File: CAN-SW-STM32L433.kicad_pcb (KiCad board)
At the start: 2 copper layers, 70 x 53 mm, 37 parts, among them J1 H GND L, J2 TERM, J3 UART1, J4 SWLINK, J5 CENTER +12V, U1 STM32L433RCT3, U2 MCP2562-E-SN

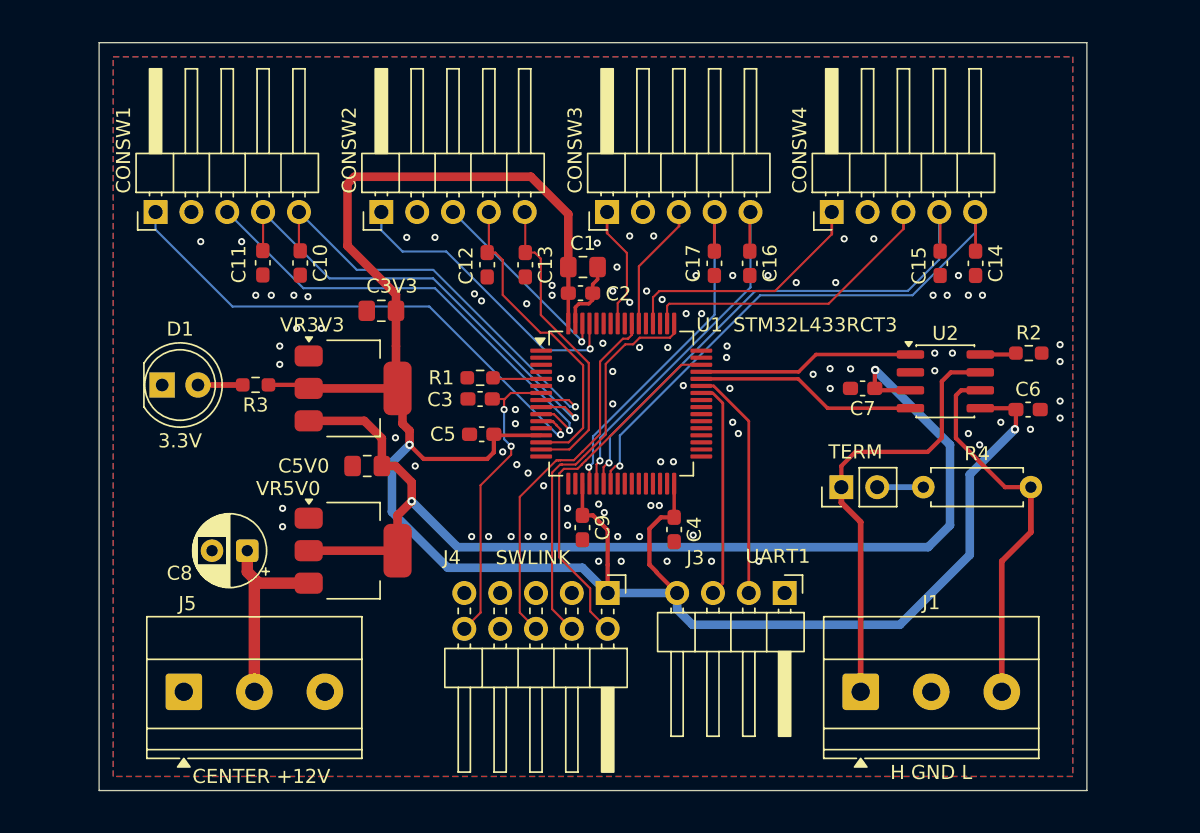
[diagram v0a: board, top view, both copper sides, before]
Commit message: added status led and tvs diode
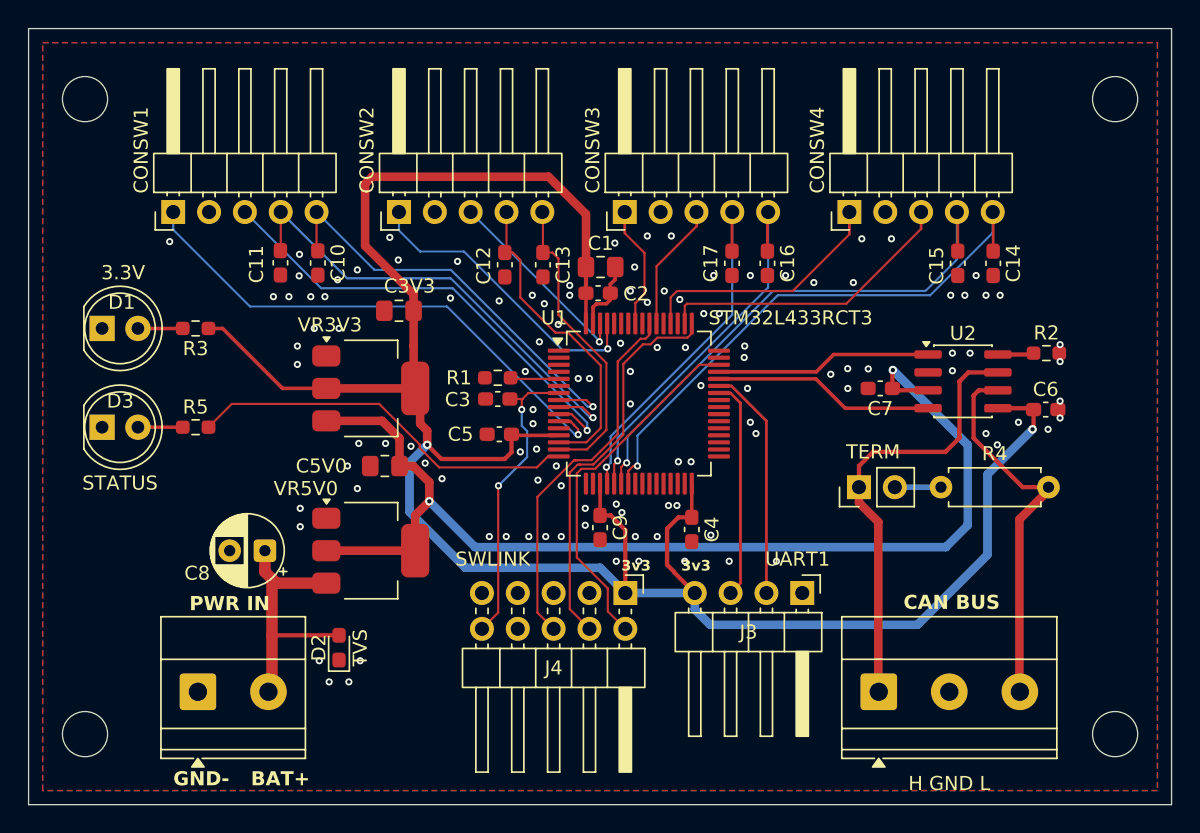
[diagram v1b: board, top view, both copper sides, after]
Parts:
- added D2: TVS, Diode_SMD:D_0603_1608Metric_Pad1.05x0.95mm_HandSolder, F.Cu at (119.0, 118.9)
- added D3: STATUS, LED_THT:LED_D5.0mm_Clear, F.Cu at (102.2, 103.2)
- added H1: MountingHole, MountingHole:MountingHole_3.2mm_M3_DIN965, F.Cu at (101.0, 80.0)
- added H2: MountingHole, MountingHole:MountingHole_3.2mm_M3_DIN965, F.Cu at (174.0, 80.0)
- added H3: MountingHole, MountingHole:MountingHole_3.2mm_M3_DIN965, F.Cu at (101.0, 125.0)
- added H4: MountingHole, MountingHole:MountingHole_3.2mm_M3_DIN965, F.Cu at (174.0, 125.0)
- added R5: 1K, Resistor_SMD:R_0603_1608Metric_Pad0.98x0.95mm_HandSolder, F.Cu at (108.8, 103.2)
- J5: value CENTER +12V -> PWR IN; footprint TerminalBlock_Phoenix:TerminalBlock_Phoenix_MKDS-1,5-3_1x03_P5.00mm_Horizontal -> TerminalBlock_Phoenix:TerminalBlock_Phoenix_MKDS-1,5-2_1x02_P5.00mm_Horizontal
- moved D1 5.85 mm to (102.2, 96.2)
- moved R3 5.84 mm to (108.8, 96.2)
- moved J1 1.28 mm to (157.2, 122.0)
- moved C1 1.25 mm to (137.5, 91.9)
- moved C10 1.25 mm to (117.5, 91.6)
- moved C11 1.25 mm to (114.8, 91.6)
- moved C12 1.25 mm to (130.8, 91.7)
- moved C13 1.25 mm to (133.4, 91.7)
- moved C14 1.25 mm to (165.4, 91.6)
- moved C15 1.25 mm to (162.8, 91.6)
- moved C16 1.25 mm to (149.4, 91.6)
- moved C17 1.25 mm to (146.8, 91.6)
- moved C2 1.25 mm to (137.4, 93.8)
- moved C3 1.25 mm to (130.2, 101.2)
- moved C3V3 1.25 mm to (123.2, 95.0)
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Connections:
- U1 pad 16: /ADC1_IN7 -> /STATUS
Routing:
- net /STATUS: track 0.00 -> 27.8 mm
- net +3.3V: track 150.7 -> 158.2 mm
- net +12V: track 14.2 -> 19.0 mm
- net Net-(D3-A): track 0.00 -> 3.17 mm
- net GND: vias 98 -> 116
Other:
- board size 70 x 53 mm -> 81 x 55 mm
- board text added: "3v3"
- board text added: "BAT+"
- board text added: "CAN BUS"
- board text added: "GND-"

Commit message: fix TVS package size, do some layout tweaks
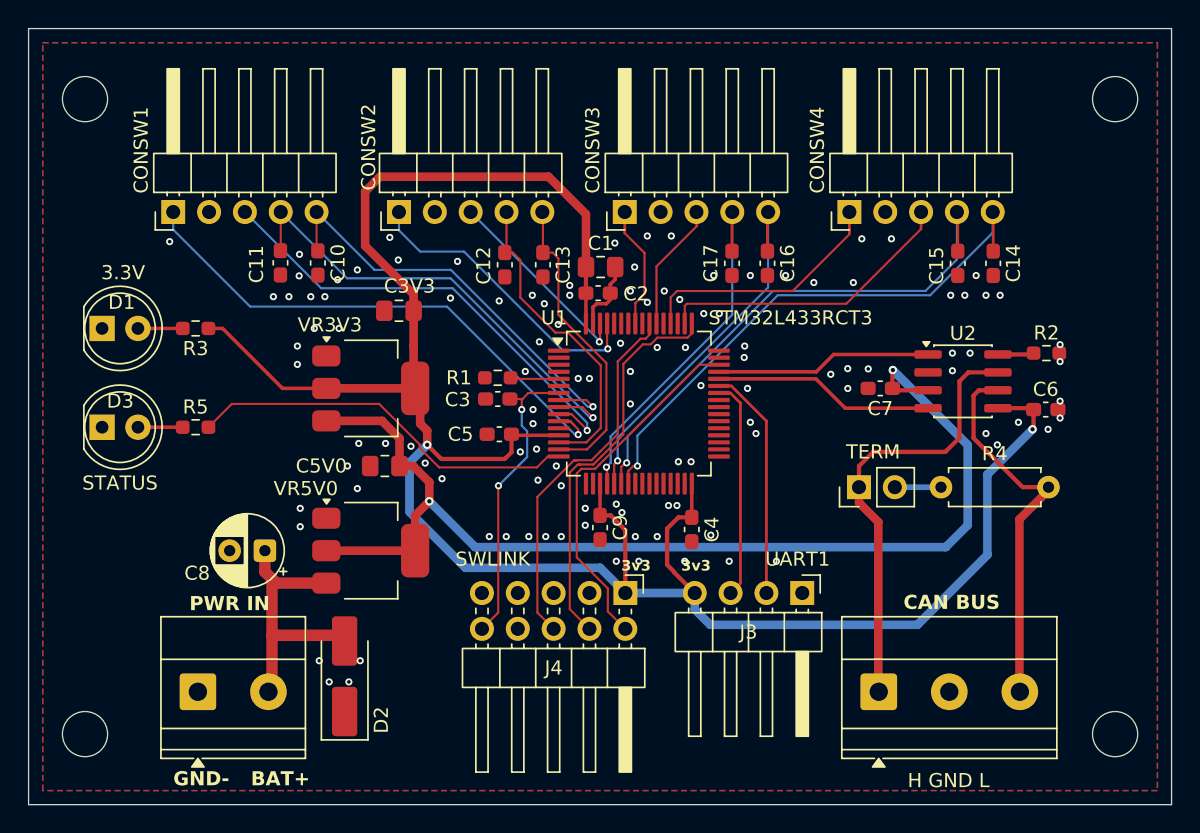
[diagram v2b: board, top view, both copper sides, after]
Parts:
- D2: footprint Diode_SMD:D_0603_1608Metric_Pad1.05x0.95mm_HandSolder -> Diode_SMD:D_SMA_Handsoldering
- moved D2 2.06 mm to (119.4, 120.9)
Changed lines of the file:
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@@
 		(tags "Through hole angled pin header THT 1x05 2.54mm single row")
 		(property "Reference" "CONSW2"
-			(at 4.385 -2.27 90)
+			(at 4.6 -2.15 90)
 			(layer "F.SilkS")
 			(effects
@@
 		)
 	)
-	(footprint "Diode_SMD:D_0603_1608Metric_Pad1.05x0.95mm_HandSolder"
+	(footprint "Diode_SMD:D_SMA_Handsoldering"
 		(layer "F.Cu")
-		(at 119 118.875 90)
-		(descr "Diode SMD 0603 (1608 Metric), square (rectangular) end terminal, IPC-7351 nominal, (Body size source: http://www.tortai-tech.com/upload/download/2011102023233369053.pdf), generated with kicad-footprint-generator")
-		(tags "diode handsolder")
+		(at 119.4 120.9 90)
+		(descr "Diode SMA (DO-214AC) Handsoldering")
+		(tags "Diode SMA (DO-214AC) Handsoldering")
 		(property "Reference" "D2"
-			(at 0 -1.43 90)
+			(at -3.1 2.6 90)
 			(layer "F.SilkS")
 			(effects
@@
 		)
 		(property "Value" "TVS"
-			(at 0 1.5 90)
-			(layer "F.SilkS")
+			(at 0 2.6 90)
+			(layer "F.Fab")
 			(effects
 				(font
@@
 		(property "Datasheet" "~"
 			(at 0 0 90)
+			(unlocked yes)
 			(layer "F.Fab")
 			(hide yes)
@@
 		(property "Description" "Bidirectional transient-voltage-suppression diode, small symbol"
 			(at 0 0 90)
+			(unlocked yes)
 			(layer "F.Fab")
 			(hide yes)
@@
 		(attr smd)
 		(fp_line
-			(start 0.8 -0.735)
-			(end -1.66 -0.735)
+			(start -4.51 -1.65)
+			(end 2.5 -1.65)
 			(stroke
 				(width 0.12)
@@
 		)
 		(fp_line
-			(start -1.66 -0.735)
-			(end -1.66 0.735)
+			(start -4.51 -1.65)
+			(end -4.51 1.65)
 			(stroke
 				(width 0.12)
@@
 		)
 		(fp_line
-			(start -1.66 0.735)
-			(end 0.8 0.735)
+			(start -4.51 1.65)
+			(end 2.5 1.65)
 			(stroke
 				(width 0.12)
@@
 			(layer "F.SilkS")
 		)
-		(fp_rect
-			(start -1.65 -0.73)
-			(end 1.65 0.73)
+		(fp_line
+			(start 4.5 -1.75)
+			(end 4.5 1.75)
 			(stroke
 				(width 0.05)
 				(type solid)
 			)
-			(fill no)
 			(layer "F.CrtYd")
 		)
 		(fp_line
-			(start 0.8 -0.4)
-			(end -0.5 -0.4)
+			(start -4.5 -1.75)
+			(end 4.5 -1.75)
+			(stroke
+				(width 0.05)
+				(type solid)
+			)
+			(layer "F.CrtYd")
+		)
+		(fp_line
+			(start 4.5 1.75)
+			(end -4.5 1.75)
+			(stroke
+				(width 0.05)
+				(type solid)
+			)
+			(layer "F.CrtYd")
+		)
+		(fp_line
+			(start -4.5 1.75)
+			(end -4.5 -1.75)
+			(stroke
+				(width 0.05)
+				(type solid)
+			)
+			(layer "F.CrtYd")
+		)
+		(fp_line
+			(start 2.3 -1.5)
+			(end -2.3 -1.5)
 			(stroke
 				(width 0.1)
@@
 		)
 		(fp_line
-			(start -0.5 -0.4)
-			(end -0.8 -0.1)
+			(start 2.3 -1.5)
+			(end 2.3 1.5)
 			(stroke
 				(width 0.1)
@@
 		)
 		(fp_line
-			(start -0.8 -0.1)
-			(end -0.8 0.4)
+			(start -0.64944 -0.79908)
+			(end -0.64944 0.80112)
 			(stroke
 				(width 0.1)
@@
 		)
 		(fp_line
-			(start 0.8 0.4)
-			(end 0.8 -0.4)
+			(start 0.50118 0.00102)
+			(end 1.4994 0.00102)
 			(stroke
 				(width 0.1)
@@
 		)
 		(fp_line
-			(start -0.8 0.4)
-			(end 0.8 0.4)
+			(start -0.64944 0.00102)
+			(end 0.50118 -0.79908)
+			(stroke
+				(width 0.1)
+				(type solid)
+			)
+			(layer "F.Fab")
+		)
+		(fp_line
+			(start -0.64944 0.00102)
+			(end -1.55114 0.00102)
+			(stroke
+				(width 0.1)
+				(type solid)
+			)
+			(layer "F.Fab")
+		)
+		(fp_line
+			(start -0.64944 0.00102)
+			(end 0.50118 0.75032)
+			(stroke
+				(width 0.1)
+				(type solid)
+			)
+			(layer "F.Fab")
+		)
+		(fp_line
+			(start 0.50118 0.75032)
+			(end 0.50118 -0.79908)
+			(stroke
+				(width 0.1)
+				(type solid)
+			)
+			(layer "F.Fab")
+		)
+		(fp_line
+			(start 2.3 1.5)
+			(end -2.3 1.5)
+			(stroke
+				(width 0.1)
+				(type solid)
+			)
+			(layer "F.Fab")
+		)
+		(fp_line
+			(start -2.3 1.5)
+			(end -2.3 -1.5)
 			(stroke
 				(width 0.1)
@@
 		)
 		(fp_text user "${REFERENCE}"
-			(at 0 0 90)
+			(at 0 -2.5 90)
 			(layer "F.Fab")
 			(effects
 				(font
-					(size 0.4 0.4)
-					(thickness 0.06)
+					(size 1 1)
+					(thickness 0.15)
 				)
 			)
 		)
 		(pad "1" smd roundrect
-			(at -0.875 0 90)
-			(size 1.05 0.95)
+			(at -2.5 0 90)
+			(size 3.5 1.8)
 			(layers "F.Cu" "F.Mask" "F.Paste")
-			(roundrect_rratio 0.25)
+			(roundrect_rratio 0.1388888889)
 			(net 6 "GND")
 			(pinfunction "A1")
@@
 		)
 		(pad "2" smd roundrect
-			(at 0.875 0 90)
-			(size 1.05 0.95)
+			(at 2.5 0 90)
+			(size 3.5 1.8)
 			(layers "F.Cu" "F.Mask" "F.Paste")
-			(roundrect_rratio 0.25)
+			(roundrect_rratio 0.1388888889)
 			(net 13 "+12V")
 			(pinfunction "A2")
@@
 		)
 		(embedded_fonts no)
-		(model "${KICAD9_3DMODEL_DIR}/Diode_SMD.3dshapes/D_0603_1608Metric.step"
+		(model "${KICAD9_3DMODEL_DIR}/Diode_SMD.3dshapes/D_SMA.step"
 			(offset
 				(xyz 0 0 0)
@@
 		)
 		(property "Value" "H GND L"
-			(at 5 6.5 0)
+			(at 4.94958 6.294395 0)
 			(layer "F.SilkS")
 			(effects
@@
 	)
 	(segment
-		(start 168.125 101.905)
-		(end 168.22 102)
-		(width 0.305)
+		(start 124.2875 93.8375)
+		(end 124.2875 95)
+		(width 0.61)
 		(layer "F.Cu")
 		(net 7)
 	)
 	(segment
-		(start 136.5 91.9)
-		(end 136.5 88.15)
+		(start 120.85 90.4)
+		(end 124.2875 93.8375)
 		(width 0.61)
 		(layer "F.Cu")
@@
 	)
 	(segment
+		(start 120.85 86.55)
+		(end 120.85 90.4)
+		(width 0.61)
+		(layer "F.Cu")
+		(net 7)
+	)
+	(segment
+		(start 168.125 101.905)
+		(end 168.22 102)
+		(width 0.305)
+		(layer "F.Cu")
+		(net 7)
+	)
+	(segment
 		(start 131.225 105.025)
 		(end 130.75 105.5)
@@
 	)
 	(segment
+		(start 136.5 91.9)
+		(end 136.5 88.15)
+		(width 0.61)
+		(layer "F.Cu")
+		(net 7)
+	)
+	(segment
 		(start 139.29 115)
 		(end 139.29 113)
@@
 	)
 	(segment
+		(start 121.9 85.5)
+		(end 120.85 86.55)
+		(width 0.61)
+		(layer "F.Cu")
+		(net 7)
+	)
+	(segment
 		(start 131.3 103.825)
 		(end 134.575 103.825)
@@
 	(segment
 		(start 133.85 85.5)
-		(end 121.35 85.5)
+		(end 121.9 85.5)
 		(width 0.61)
 		(layer "F.Cu")
@@
 	)
 	(segment
-		(start 121.35 85.5)
-		(end 120.85 86)
-		(width 0.61)
-		(layer "F.Cu")
-		(net 7)
-	)
-	(segment
 		(start 131.225 103.75)
 		(end 131.3 103.825)
@@
 	)
 	(segment
-		(start 124.2875 93.8375)
-		(end 120.85 90.4)
-		(width 0.61)
-		(layer "F.Cu")
-		(net 7)
-	)
-	(segment
-		(start 124.2875 95)
-		(end 124.2875 93.8375)
+		(start 136.5 88.15)
+		(end 133.85 85.5)
 		(width 0.61)
 		(layer "F.Cu")
@@
 	)
 	(segment
-		(start 120.85 86)
-		(end 120.85 90.4)
-		(width 0.61)
-		(layer "F.Cu")
-		(net 7)
-	)
-	(segment
 		(start 139.29 110.54)
 		(end 139.29 113)
@@
 	)
 	(segment
-		(start 136.5 88.15)
-		(end 133.85 85.5)
-		(width 0.61)
-		(layer "F.Cu")
-		(net 7)
-	)
-	(segment
 		(start 168.22 103.33)
 		(end 168.15 103.4)
@@
 		(start 119 118)
 		(end 114.25 118)
-		(width 0.305)
+		(width 0.8128)
 		(layer "F.Cu")
 		(net 13)

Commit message: layout tweak
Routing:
- net GND: vias 116 -> 120
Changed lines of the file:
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@@
 	)
 	(via
-		(at 120.5 119.8)
+		(at 121.5 123.4)
 		(size 0.508)
 		(drill 0.254)
@@
 	)
 	(via
-		(at 119.7 121.3)
+		(at 119.4 126.1)
 		(size 0.508)
 		(drill 0.254)
@@
 	)
 	(via
+		(at 117.9 117)
+		(size 0.508)
+		(drill 0.254)
+		(layers "F.Cu" "B.Cu")
+		(free yes)
+		(net 6)
+	)
+	(via
 		(at 164.85 93.9)
 		(size 0.508)
@@
 	)
 	(via
+		(at 117.9 119)
+		(size 0.508)
+		(drill 0.254)
+		(layers "F.Cu" "B.Cu")
+		(free yes)
+		(net 6)
+	)
+	(via
 		(at 140 111)
 		(size 0.508)
@@
 	)
 	(via
-		(at 118.3 121.3)
+		(at 117.3 123.4)
 		(size 0.508)
 		(drill 0.254)
@@
 	)
 	(via
+		(at 115.2 115.2)
+		(size 0.508)
+		(drill 0.254)
+		(layers "F.Cu" "B.Cu")
+		(free yes)
+		(net 6)
+	)
+	(via
 		(at 134.75 111)
 		(size 0.508)
@@
 	)
 	(via
-		(at 117.6 119.8)
+		(at 115.2 119)
 		(size 0.508)
 		(drill 0.254)
@@
 		(size 0.508)
 		(drill 0.254)
+		(layers "F.Cu" "B.Cu")
+		(free yes)
+		(net 6)
+	)
+	(via
+		(at 115.2 117)
+		(size 0.508)
+		(drill 0.254)
